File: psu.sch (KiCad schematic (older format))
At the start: 30 parts, among them U2 LM5017MR, U3 TPS76333

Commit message: Adding LCSC part numbers
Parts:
- C16: LCSC (none) -> C28233
- C17, C18: LCSC (none) -> C13832
- C19, C20: LCSC (none) -> C15849
- C21: LCSC (none) -> C57112
- C22: LCSC (none) -> C1779
- C23: LCSC (none) -> C1525
- C24: LCSC (none) -> C26404
- C25, C26, C27, C28: LCSC (none) -> C13585
- D6: LCSC (none) -> C126484
- R28: LCSC (none) -> C22859
- R29: LCSC (none) -> C4147
- R30, R33: LCSC (none) -> C25900
- R31: LCSC (none) -> C25741
- R32: LCSC (none) -> C25779
- R34: LCSC (none) -> C25752
- R35: LCSC (none) -> C51721
- U2: LCSC (none) -> C34355
- U3: LCSC (none) -> C160916
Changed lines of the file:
@@
 F 2 "Package_SO:SOIC-8-1EP_3.9x4.9mm_P1.27mm_EP2.95x4.9mm_Mask2.71x3.4mm_ThermalVias" H 5050 2150 50  0001 L CIN
 F 3 "http://www.ti.com/lit/ds/symlink/lm5017.pdf" H 5000 2600 50  0001 C CNN
+F 4 "C34355" H 5000 2600 50  0001 C CNN "LCSC"
 	1    5000 2600
 	1    0    0    -1
@@
 F 2 "Resistor_SMD:R_0402_1005Metric" V 3880 2600 50  0001 C CNN
 F 3 "~" H 3950 2600 50  0001 C CNN
+F 4 "C4147" H 3950 2600 50  0001 C CNN "LCSC"
 	1    3950 2600
 	1    0    0    -1
@@
 F 2 "Resistor_SMD:R_0402_1005Metric" V 3880 3100 50  0001 C CNN
 F 3 "~" H 3950 3100 50  0001 C CNN
+F 4 "C25900" H 3950 3100 50  0001 C CNN "LCSC"
 	1    3950 3100
 	1    0    0    -1
@@
 F 2 "Capacitor_SMD:C_0603_1608Metric" H 4938 4900 50  0001 C CNN
 F 3 "~" H 4900 5050 50  0001 C CNN
+F 4 "C15849" H 4900 5050 50  0001 C CNN "LCSC"
 	1    4900 5050
 	-1   0    0    -1
@@
 F 2 "Capacitor_SMD:C_0805_2012Metric" H 5938 5050 50  0001 C CNN
 F 3 "~" H 5900 5200 50  0001 C CNN
+F 4 "C1779" H 5900 5200 50  0001 C CNN "LCSC"
 	1    5900 5200
 	-1   0    0    -1
@@
 F 2 "Package_TO_SOT_SMD:SOT-23-5" H 5500 5225 50  0001 C CIN
 F 3 "http://www.ti.com/lit/ds/symlink/tps763.pdf" H 5500 4900 50  0001 C CNN
+F 4 "C160916" H 5500 4900 50  0001 C CNN "LCSC"
 	1    5500 4900
 	1    0    0    -1
@@
 F 2 "Capacitor_SMD:C_0603_1608Metric" H 5688 2250 50  0001 C CNN
 F 3 "~" H 5650 2400 50  0001 C CNN
+F 4 "C57112" H 5650 2400 50  0001 C CNN "LCSC"
 	1    5650 2400
 	0    1    1    0
@@
 F 2 "Capacitor_SMD:C_0603_1608Metric" H 5538 3000 50  0001 C CNN
 F 3 "~" H 5500 3150 50  0001 C CNN
+F 4 "C15849" H 5500 3150 50  0001 C CNN "LCSC"
 	1    5500 3150
 	1    0    0    -1
@@
 F 2 "Resistor_SMD:R_0402_1005Metric" V 7230 2750 50  0001 C CNN
 F 3 "~" H 7300 2750 50  0001 C CNN
+F 4 "C25752" H 7300 2750 50  0001 C CNN "LCSC"
 	1    7300 2750
 	1    0    0    -1
@@
 F 2 "Resistor_SMD:R_0402_1005Metric" V 7230 3150 50  0001 C CNN
 F 3 "~" H 7300 3150 50  0001 C CNN
+F 4 "C51721" H 7300 3150 50  0001 C CNN "LCSC"
 	1    7300 3150
 	1    0    0    -1
@@
 F 2 "Capacitor_SMD:C_1206_3216Metric" H 8138 3000 50  0001 C CNN
 F 3 "~" H 8100 3150 50  0001 C CNN
+F 4 "C13585" H 8100 3150 50  0001 C CNN "LCSC"
 	1    8100 3150
 	1    0    0    -1
@@
 F 2 "Capacitor_SMD:C_0805_2012Metric" H 2738 2500 50  0001 C CNN
 F 3 "~" H 2700 2650 50  0001 C CNN
+F 4 "C28233" H 2700 2650 50  0001 C CNN "LCSC"
 	1    2700 2650
 	1    0    0    -1
@@
 F 2 "Capacitor_SMD:C_1206_3216Metric" H 3238 2500 50  0001 C CNN
 F 3 "~" H 3200 2650 50  0001 C CNN
+F 4 "C13832" H 3200 2650 50  0001 C CNN "LCSC"
 	1    3200 2650
 	1    0    0    -1
@@
 F 2 "Resistor_SMD:R_0603_1608Metric" V 2880 2400 50  0001 C CNN
 F 3 "~" H 2950 2400 50  0001 C CNN
+F 4 "C22859" H 2950 2400 50  0001 C CNN "LCSC"
 	1    2950 2400
 	0    1    1    0
@@
 F 2 "Capacitor_SMD:C_1206_3216Metric" H 3638 2500 50  0001 C CNN
 F 3 "~" H 3600 2650 50  0001 C CNN
+F 4 "C13832" H 3600 2650 50  0001 C CNN "LCSC"
 	1    3600 2650
 	1    0    0    -1
@@
 F 2 "Inductor_SMD:L_Bourns_SRF1260" H 6450 2400 50  0001 C CNN
 F 3 "~" H 6450 2400 50  0001 C CNN
+F 4 "" H 6450 2400 50  0001 C CNN "LCSC"
 	1    6450 2400
 	1    0    0    -1
@@
 F 2 "Capacitor_SMD:C_0402_1005Metric" H 6688 2650 50  0001 C CNN
 F 3 "~" H 6650 2800 50  0001 C CNN
+F 4 "C26404" H 6650 2800 50  0001 C CNN "LCSC"
 	1    6650 2800
 	0    1    1    0
@@
 F 2 "Resistor_SMD:R_0402_1005Metric" V 6180 2800 50  0001 C CNN
 F 3 "~" H 6250 2800 50  0001 C CNN
+F 4 "C25779" H 6250 2800 50  0001 C CNN "LCSC"
 	1    6250 2800
 	0    1    1    0
@@
 F 2 "Capacitor_SMD:C_0402_1005Metric" H 6488 2900 50  0001 C CNN
 F 3 "~" H 6450 3050 50  0001 C CNN
+F 4 "C1525" H 6450 3050 50  0001 C CNN "LCSC"
 	1    6450 3050
 	1    0    0    -1
@@
 F 2 "Capacitor_SMD:C_1206_3216Metric" H 7538 1950 50  0001 C CNN
 F 3 "~" H 7500 2100 50  0001 C CNN
+F 4 "C13585" H 7500 2100 50  0001 C CNN "LCSC"
 	1    7500 2100
 	1    0    0    -1
@@
 F 2 "Diode_SMD:D_SOD-123" V 7100 1650 50  0001 C CNN
 F 3 "~" V 7100 1650 50  0001 C CNN
+F 4 "C126484" H 7100 1650 50  0001 C CNN "LCSC"
 	1    7100 1650
 	-1   0    0    -1
@@
 F 2 "Resistor_SMD:R_0402_1005Metric" V 4280 2500 50  0001 C CNN
 F 3 "~" H 4350 2500 50  0001 C CNN
+F 4 "C25741" H 4350 2500 50  0001 C CNN "LCSC"
 	1    4350 2500
 	0    -1   -1   0
@@
 F 2 "Capacitor_SMD:C_1206_3216Metric" H 7938 1750 50  0001 C CNN
 F 3 "~" H 7900 1900 50  0001 C CNN
+F 4 "C13585" H 7900 1900 50  0001 C CNN "LCSC"
 	1    7900 1900
 	1    0    0    -1
@@
 F 2 "Capacitor_SMD:C_1206_3216Metric" H 7738 2600 50  0001 C CNN
 F 3 "~" H 7700 2750 50  0001 C CNN
+F 4 "C13585" H 7700 2750 50  0001 C CNN "LCSC"
 	1    7700 2750
 	1    0    0    -1
@@
 F 2 "TestPoint:TestPoint_Pad_D1.5mm" H 8400 1650 50  0001 C CNN
 F 3 "~" H 8400 1650 50  0001 C CNN
+F 4 "~" H 8200 1650 50  0001 C CNN "LCSC"
 	1    8200 1650
 	0    1    -1   0
@@
 F 2 "TestPoint:TestPoint_Pad_D1.5mm" H 8400 2500 50  0001 C CNN
 F 3 "~" H 8400 2500 50  0001 C CNN
+F 4 "~" H 8200 2500 50  0001 C CNN "LCSC"
 	1    8200 2500
 	0    1    -1   0
@@
 F 2 "TestPoint:TestPoint_Pad_D1.5mm" H 2800 2400 50  0001 C CNN
 F 3 "~" H 2800 2400 50  0001 C CNN
+F 4 "~" H 2600 2400 50  0001 C CNN "LCSC"
 	1    2600 2400
 	0    -1   -1   0
@@
 F 2 "TestPoint:TestPoint_Pad_D1.5mm" H 6800 4800 50  0001 C CNN
 F 3 "~" H 6800 4800 50  0001 C CNN
+F 4 "~" H 6600 4800 50  0001 C CNN "LCSC"
 	1    6600 4800
 	0    1    -1   0
@@
 F 2 "Resistor_SMD:R_0402_1005Metric" V 6380 5050 50  0001 C CNN
 F 3 "~" H 6450 5050 50  0001 C CNN
+F 4 "C25900" H 6450 5050 50  0001 C CNN "LCSC"
 	1    6450 5050
 	1    0    0    -1

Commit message: Tweaked LM5017 package
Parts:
- U2: footprint Package_SO:SOIC-8-1EP_3.9x4.9mm_P1.27mm_EP2.95x4.9mm_Mask2.71x3.4mm_ThermalVias -> Package_SO:SOIC-8-1EP_3.9x4.9mm_P1.27mm_EP2.41x3.3mm
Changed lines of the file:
@@
 F 0 "U2" H 5000 3067 50  0000 C CNN
 F 1 "LM5017MR" H 5000 2976 50  0000 C CNN
-F 2 "Package_SO:SOIC-8-1EP_3.9x4.9mm_P1.27mm_EP2.95x4.9mm_Mask2.71x3.4mm_ThermalVias" H 5050 2150 50  0001 L CIN
+F 2 "Package_SO:SOIC-8-1EP_3.9x4.9mm_P1.27mm_EP2.41x3.3mm" H 5050 2150 50  0001 L CIN
 F 3 "http://www.ti.com/lit/ds/symlink/lm5017.pdf" H 5000 2600 50  0001 C CNN
 F 4 "C34355" H 5000 2600 50  0001 C CNN "LCSC"

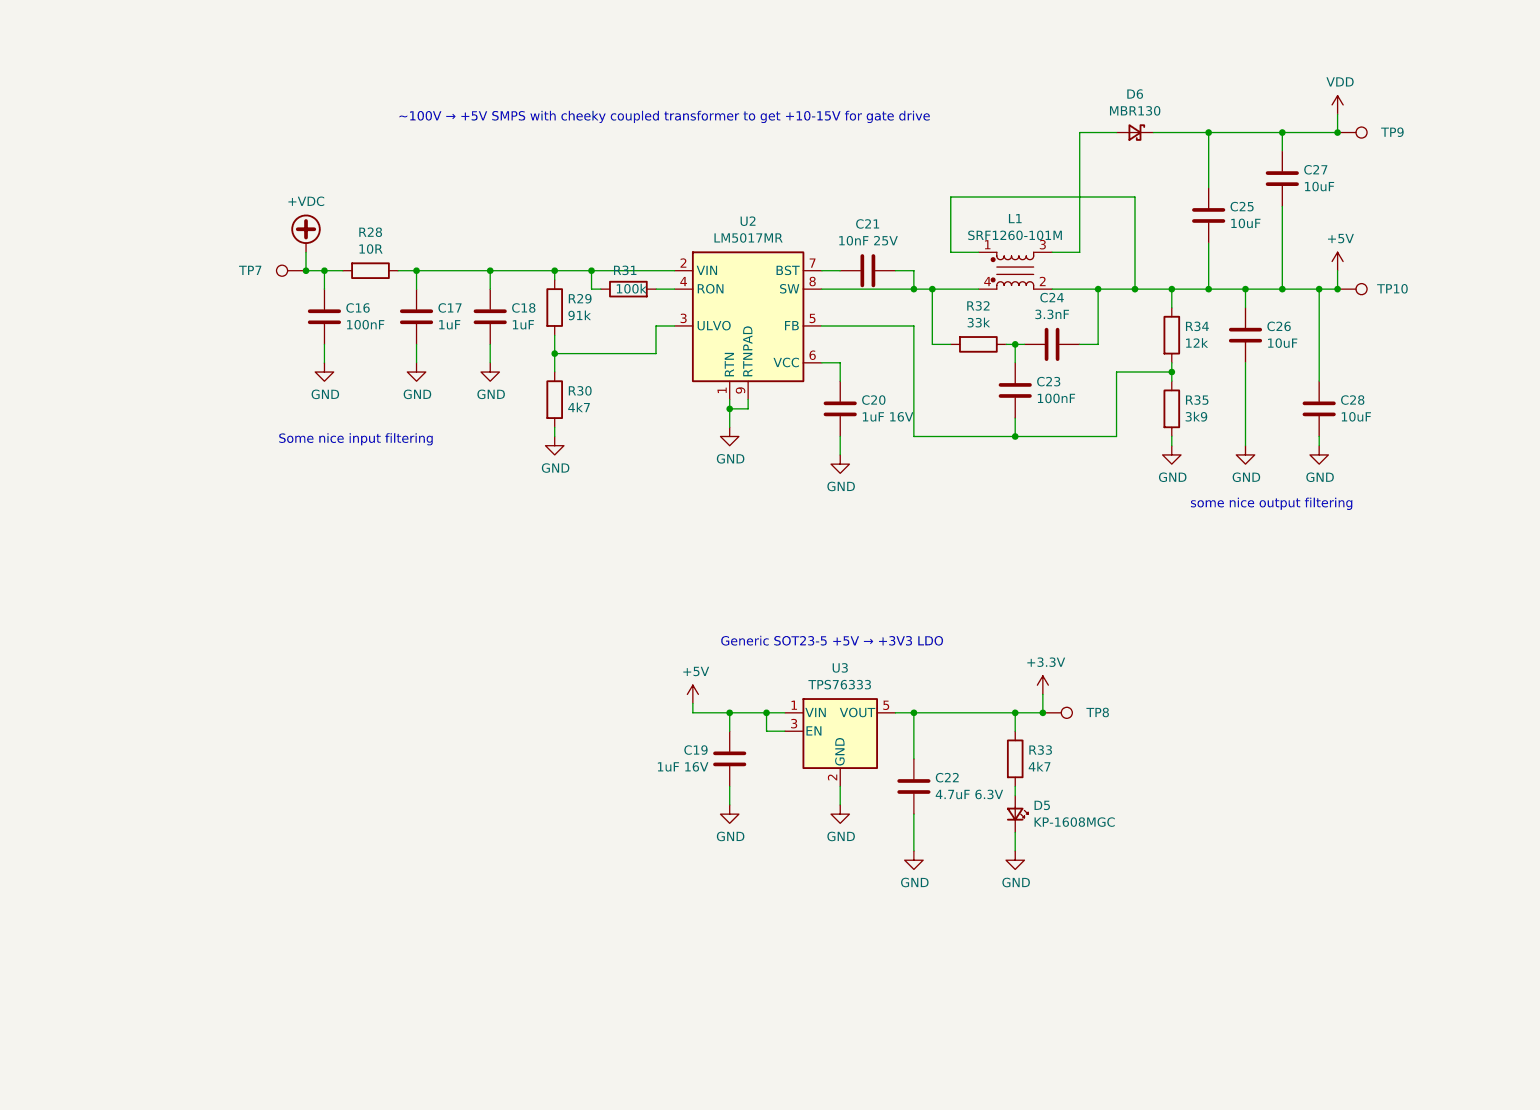
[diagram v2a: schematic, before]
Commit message: Removed coupled inductor
Added TPS61041DB
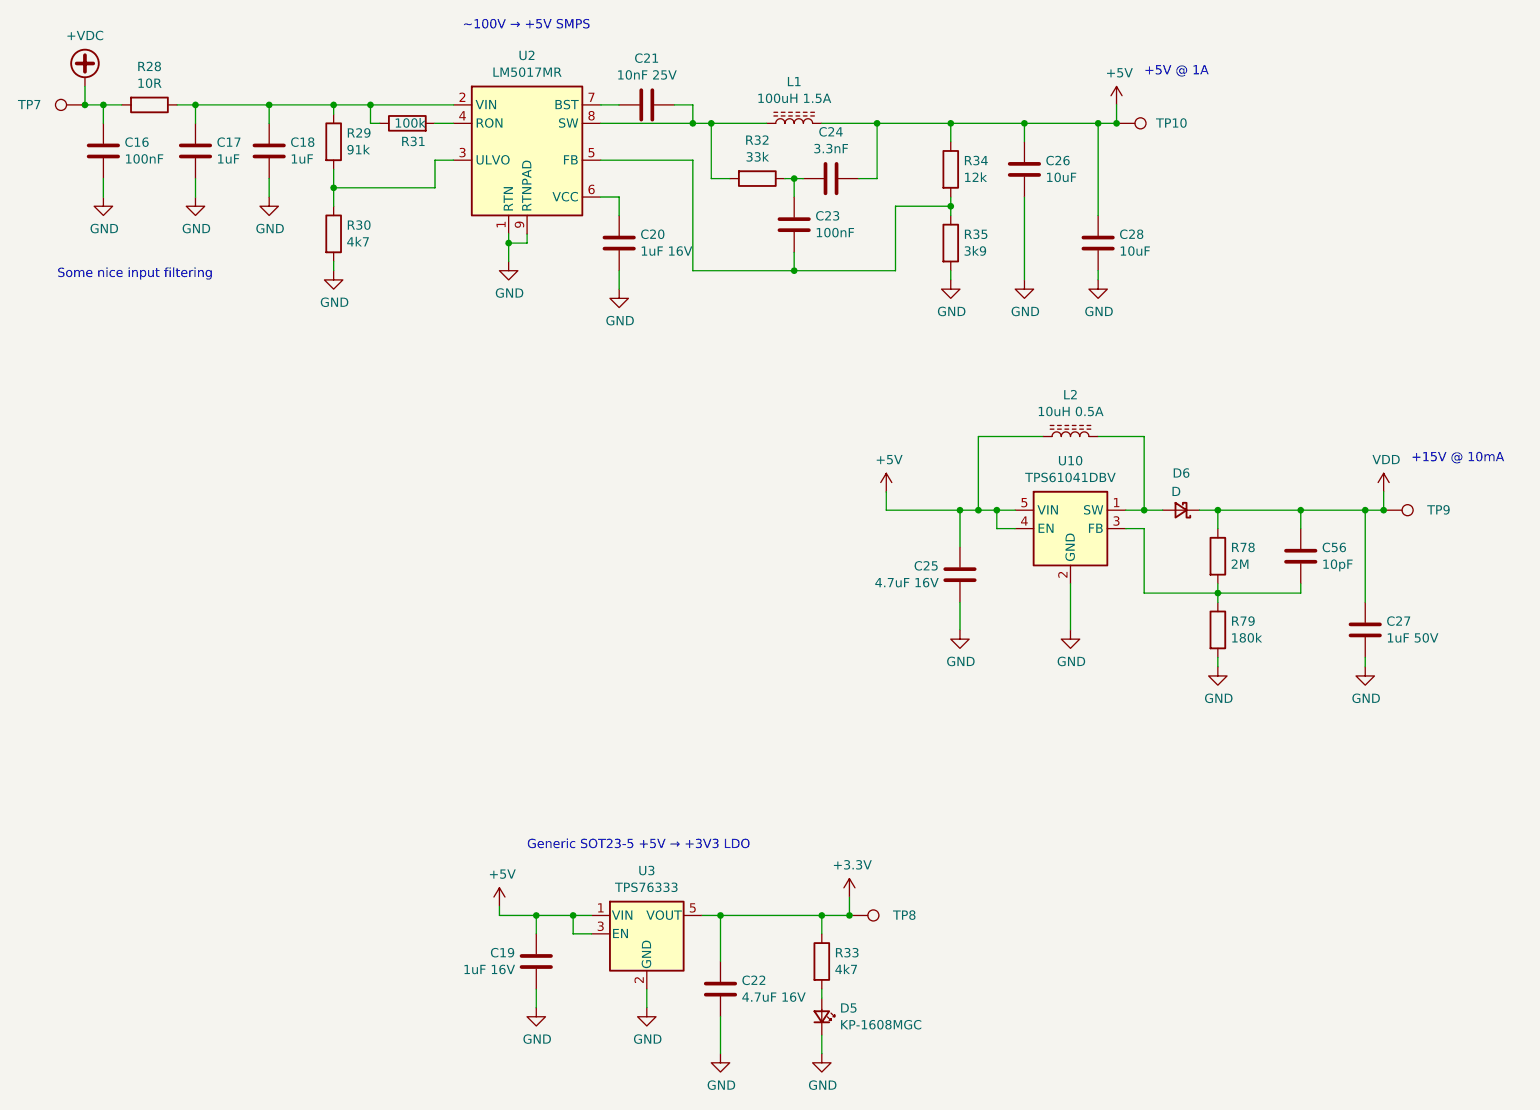
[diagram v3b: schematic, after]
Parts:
- removed L1: SRF1260-101M, Inductor_SMD:L_Bourns_SRF1260, symbol Device:L_Core_Iron_Coupled_1342
- added C56: 10pF, Capacitor_SMD:C_0402_1005Metric, symbol Device:C
- added L1: 100uH 1.5A, Inductor_SMD:L_Wuerth_HCI-1040, symbol Device:L_Core_Ferrite
- added L2: 10uH 0.5A, Inductor_SMD:L_0805_2012Metric, symbol Device:L_Core_Ferrite
- added R78: 2M, Resistor_SMD:R_0402_1005Metric, symbol Device:R
- added R79: 180k, Resistor_SMD:R_0402_1005Metric, symbol Device:R
- added U10: TPS61041DBV, Package_TO_SOT_SMD:SOT-23-5, symbol Regulator_Switching:TPS61041DBV
- C22: value 4.7uF 6.3V -> 4.7uF 16V; footprint Capacitor_SMD:C_0805_2012Metric -> Capacitor_SMD:C_0603_1608Metric; LCSC C1779 -> C19666
- C25: value 10uF -> 4.7uF 16V; footprint Capacitor_SMD:C_1206_3216Metric -> Capacitor_SMD:C_0603_1608Metric; LCSC C13585 -> C19666
- C27: value 10uF -> 1uF 50V; footprint Capacitor_SMD:C_1206_3216Metric -> Capacitor_SMD:C_0603_1608Metric; LCSC C13585 -> C15849
- D6: value MBR130 -> D; footprint Diode_SMD:D_SOD-123 -> Diode_SMD:D_SOD-323; LCSC C126484 -> (none)
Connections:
- net +5V: now also C25.1, L1.2, L2.1, U10.4 (EN), U10.5 (VIN); no longer C25.2, C27.2
- net GND: now also C25.2, C27.2, R79.2, U10.2 (GND)
- net VDD: now also C56.1, R78.1; no longer C25.1
- net at C21.1, R32.2, U2.8 (SW): now also L1.1
- net at D6.2 (A): now also L2.2, U10.1 (SW)
- new net: C56.2, R78.2, R79.1, U10.3 (FB)
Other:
- note added: "+15V @ 10mA"
- note added: "+5V @ 1A"
- note added: "~~100V → +5V SMPS\n"
- note removed: "some nice output filtering"
- note removed: "~~100V → +5V SMPS with cheeky coupled transformer to get +10-15V for gate drive"
- moved on the sheet: C16, C17, C18, C19, C20, C21, C22, C23, C24, C25, C26, C27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

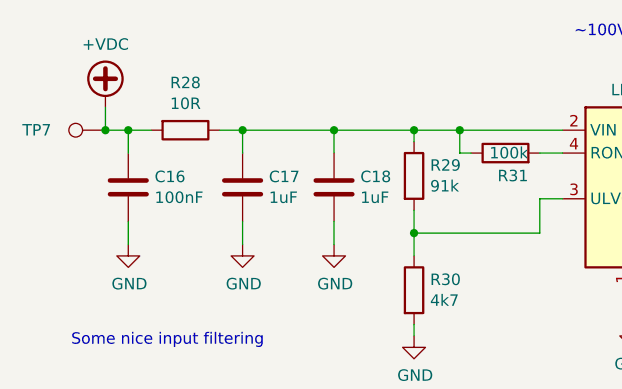
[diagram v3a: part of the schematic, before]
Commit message: Tweaking potential dividers
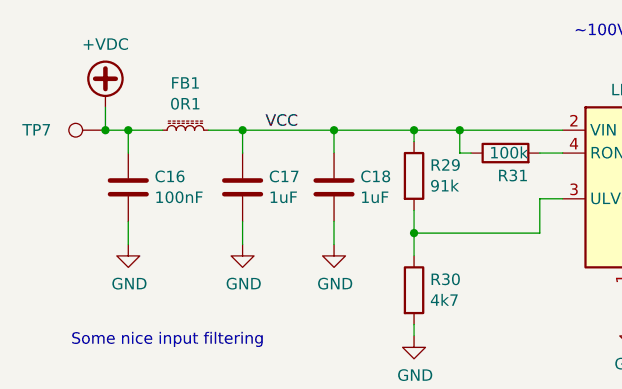
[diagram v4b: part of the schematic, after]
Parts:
- removed R28: 10R, Resistor_SMD:R_0603_1608Metric, symbol Device:R
- added FB1: 0R1, Inductor_SMD:L_0603_1608Metric, symbol Device:L_Core_Ferrite_Small
- R29: footprint Resistor_SMD:R_0402_1005Metric -> Resistor_SMD:R_0603_1608Metric; LCSC C4147 -> (none)
- R30: footprint Resistor_SMD:R_0402_1005Metric -> Resistor_SMD:R_0603_1608Metric; LCSC C25900 -> (none)
- R31: footprint Resistor_SMD:R_0402_1005Metric -> Resistor_SMD:R_0603_1608Metric; LCSC C25741 -> (none)
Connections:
- net +VDC: now also FB1.1
- net VCC: now reaches C17.1, C18.1, R29.1, R31.1, U2.2 (VIN)
- net VCC: now also FB1.2
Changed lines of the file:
@@
 F 0 "R29" H 2820 1746 50  0000 L CNN
 F 1 "91k" H 2820 1655 50  0000 L CNN
-F 2 "Resistor_SMD:R_0402_1005Metric" V 2680 1700 50  0001 C CNN
+F 2 "Resistor_SMD:R_0603_1608Metric" V 2680 1700 50  0001 C CNN
 F 3 "~" H 2750 1700 50  0001 C CNN
-F 4 "C4147" H 2750 1700 50  0001 C CNN "LCSC"
+F 4 "" H 2750 1700 50  0001 C CNN "LCSC"
 	1    2750 1700
 	1    0    0    -1
@@
 F 0 "R30" H 2820 2246 50  0000 L CNN
 F 1 "4k7" H 2820 2155 50  0000 L CNN
-F 2 "Resistor_SMD:R_0402_1005Metric" V 2680 2200 50  0001 C CNN
+F 2 "Resistor_SMD:R_0603_1608Metric" V 2680 2200 50  0001 C CNN
 F 3 "~" H 2750 2200 50  0001 C CNN
-F 4 "C25900" H 2750 2200 50  0001 C CNN "LCSC"
+F 4 "" H 2750 2200 50  0001 C CNN "LCSC"
 	1    2750 2200
 	1    0    0    -1
@@
 	1    0    0    -1
 $EndComp
-$Comp
-L Device:R R28
-U 1 1 6138E5EE
-P 1750 1500
-F 0 "R28" V 1543 1500 50  0000 C CNN
-F 1 "10R" V 1634 1500 50  0000 C CNN
-F 2 "Resistor_SMD:R_0603_1608Metric" V 1680 1500 50  0001 C CNN
-F 3 "~" H 1750 1500 50  0001 C CNN
-F 4 "C22859" H 1750 1500 50  0001 C CNN "LCSC"
-	1    1750 1500
-	0    1    1    0
-$EndComp
 Wire Wire Line
 	1500 1900 1500 2000
@@
 Connection ~ 2000 1500
 Wire Wire Line
-	2000 1500 1900 1500
-Wire Wire Line
 	1500 1600 1500 1500
-Wire Wire Line
-	1500 1500 1600 1500
 Wire Wire Line
 	1500 1500 1400 1500
@@
 F 0 "R31" V 3050 1500 50  0000 L CNN
 F 1 "100k" V 3150 1500 50  0000 L CNN
-F 2 "Resistor_SMD:R_0402_1005Metric" V 3080 1600 50  0001 C CNN
+F 2 "Resistor_SMD:R_0603_1608Metric" V 3080 1600 50  0001 C CNN
 F 3 "~" H 3150 1600 50  0001 C CNN
-F 4 "C25741" H 3150 1600 50  0001 C CNN "LCSC"
+F 4 "" H 3150 1600 50  0001 C CNN "LCSC"
 	1    3150 1600
 	0    -1   -1   0
@@
 Text Notes 7150 1350 0    50   ~ 0
 +5V @ 1A
+$Comp
+L Device:L_Core_Ferrite_Small FB1
+U 1 1 60931CAF
+P 1750 1500
+F 0 "FB1" V 1955 1500 50  0000 C CNN
+F 1 "0R1" V 1864 1500 50  0000 C CNN
+F 2 "Inductor_SMD:L_0603_1608Metric" H 1750 1500 50  0001 C CNN
+F 3 "~" H 1750 1500 50  0001 C CNN
+F 4 "C80165" V 1750 1500 50  0001 C CNN "LCSC"
+	1    1750 1500
+	0    -1   -1   0
+$EndComp
+Wire Wire Line
+	1850 1500 2000 1500
+Wire Wire Line
+	1500 1500 1650 1500
+Text Label 2100 1500 0    50   ~ 0
+VCC
 $EndSCHEMATC
